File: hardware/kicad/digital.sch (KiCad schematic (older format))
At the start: 0 parts

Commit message: Added Modex library and hierarchial sheets for power, analog and digital circuitry.
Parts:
- added U?: DSPIC33FJ128GP204, QFN/TQFP44, symbol DSPIC33FJ128GP204
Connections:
- net labels added: p3v3
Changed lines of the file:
@@
 LIBS:valves
 LIBS:microchip_dspic33dsc
+LIBS:modex
 LIBS:ultrasonic_anemometer-cache
 EELAYER 25 0
@@
 $Descr A4 11693 8268
 encoding utf-8
-Sheet 1 4
+Sheet 4 4
 Title ""
 Date ""
@@
 Comment4 ""
 $EndDescr
+Text HLabel 4850 1950 0    60   Input ~ 0
+p3v3
+$Comp
+L DSPIC33FJ128GP204 U?
+U 1 1 57FA7486
+P 6250 4300
+F 0 "U?" H 5100 6350 50  0000 L CNN
+F 1 "DSPIC33FJ128GP204" H 5100 6250 50  0000 L CNN
+F 2 "QFN/TQFP44" H 6250 3500 50  0000 C CIN
+F 3 "" H 5550 3900 50  0000 C CNN
+	1    6250 4300
+	1    0    0    -1
+$EndComp
 $EndSCHEMATC

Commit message: Added symbol for DSPIC
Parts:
- removed U?: DSPIC33FJ128GP204, QFN/TQFP44, symbol DSPIC33FJ128GP204
- added U?: DSPIC33EP512GP504, QFN/TQFP44, symbol DSPIC33EP512GP504
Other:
- note added: "33EP512GP504-IPT"
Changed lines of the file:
@@
 Text HLabel 4850 1950 0    60   Input ~ 0
 p3v3
+Text Notes 1950 1700 0    60   ~ 0
+33EP512GP504-IPT
 $Comp
-L DSPIC33FJ128GP204 U?
-U 1 1 57FA7486
-P 6250 4300
-F 0 "U?" H 5100 6350 50  0000 L CNN
-F 1 "DSPIC33FJ128GP204" H 5100 6250 50  0000 L CNN
-F 2 "QFN/TQFP44" H 6250 3500 50  0000 C CIN
-F 3 "" H 5550 3900 50  0000 C CNN
-	1    6250 4300
+L DSPIC33EP512GP504 U?
+U 1 1 584BE23E
+P 6350 4100
+F 0 "U?" H 5200 6150 50  0000 L CNN
+F 1 "DSPIC33EP512GP504" H 5200 6050 50  0000 L CNN
+F 2 "QFN/TQFP44" H 6350 3300 50  0000 C CIN
+F 3 "" H 5650 3700 50  0000 C CNN
+	1    6350 4100
 	1    0    0    -1
 $EndComp

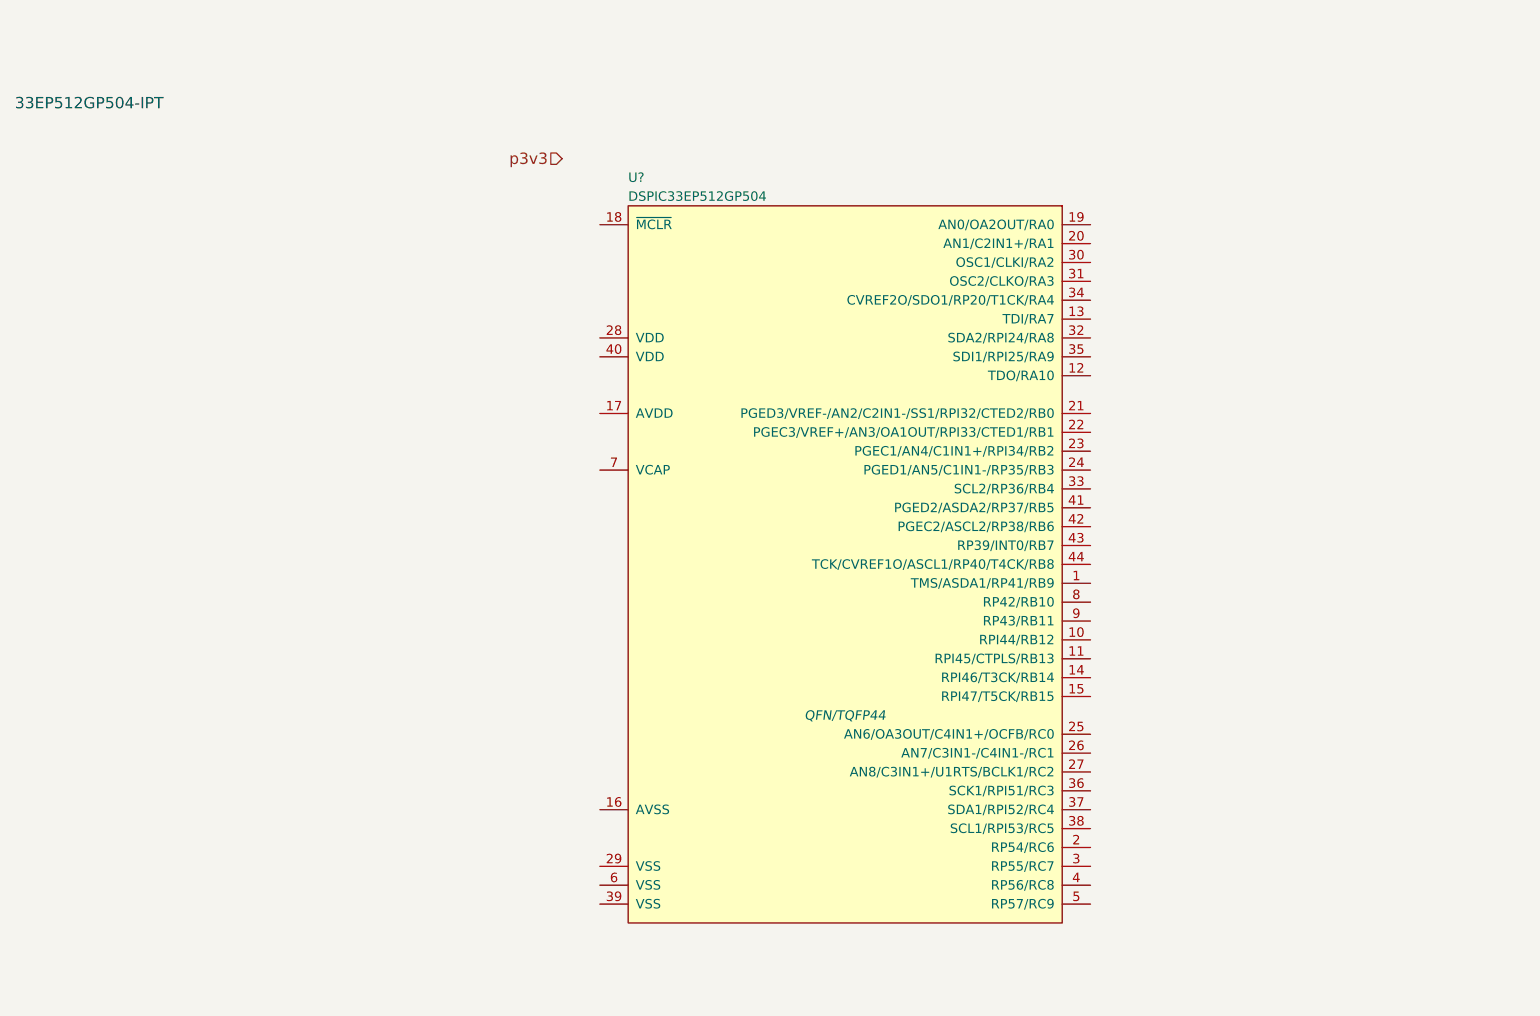
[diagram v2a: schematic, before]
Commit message: Updated schematic and PCB.
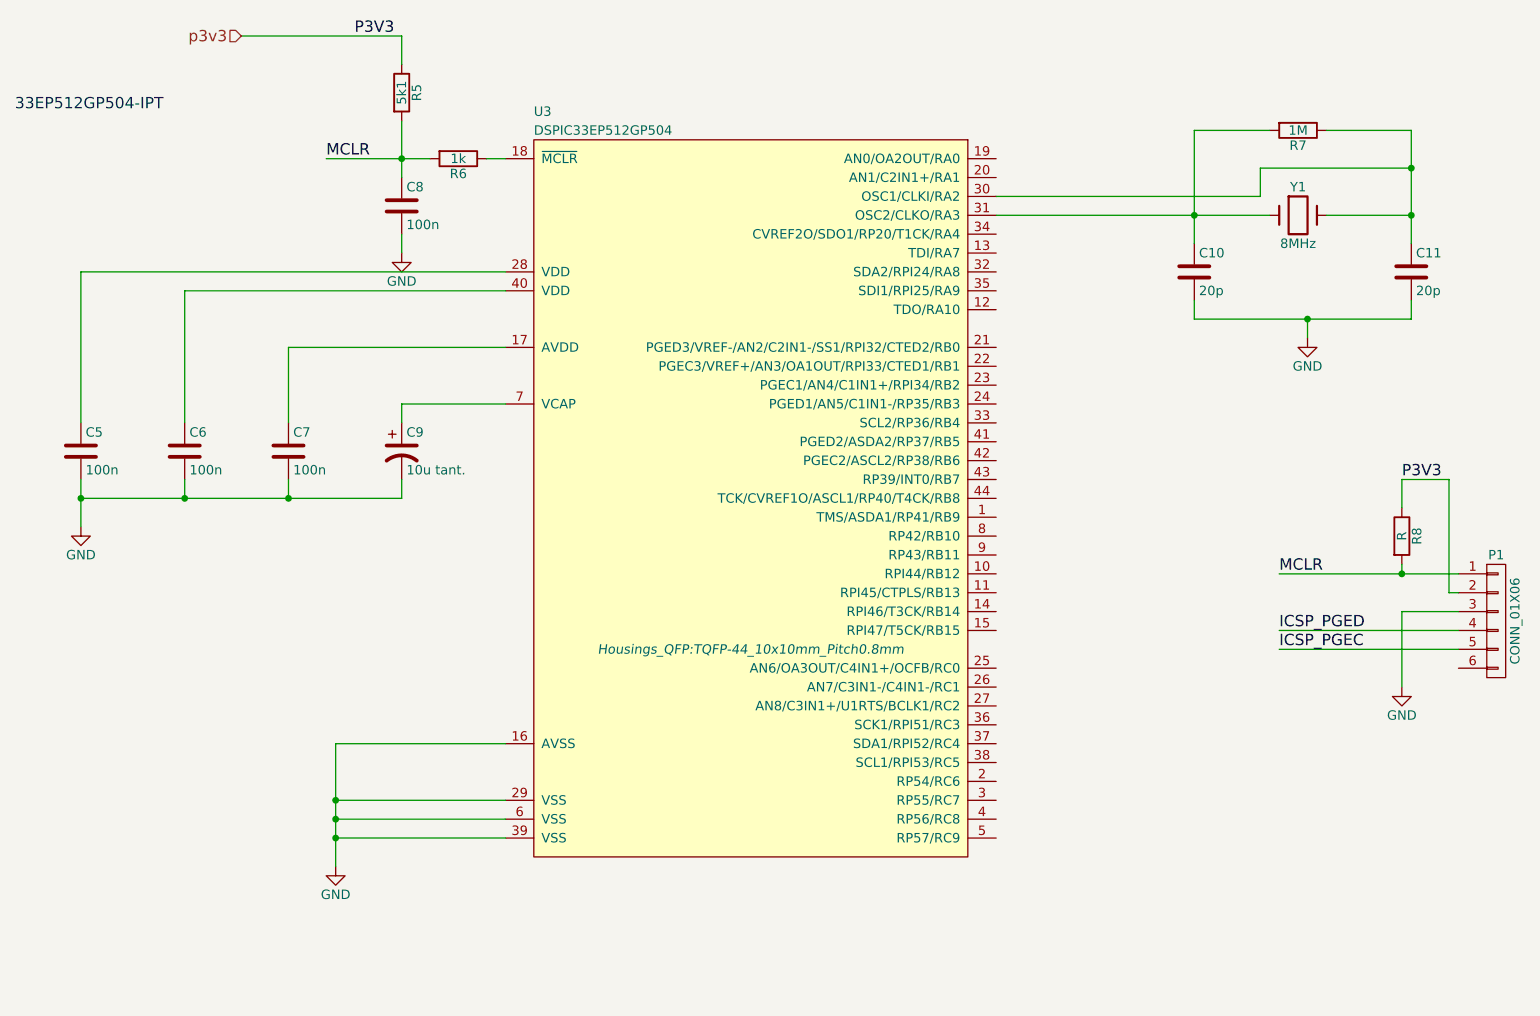
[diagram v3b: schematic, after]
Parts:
- removed U?: DSPIC33EP512GP504, QFN/TQFP44, symbol DSPIC33EP512GP504
- added C10, C11: 20p, Capacitors_SMD:C_0805_HandSoldering, symbol C
- added C5, C6, C7, C8: 100n, Capacitors_SMD:C_0805_HandSoldering, symbol C
- added C9: 10u tant., SMD_Packages:SMD-1206_Pol, symbol CP1
- added P1: CONN_01X06, Pin_Headers:Pin_Header_Straight_1x06, symbol CONN_01X06
- added R5: 5k1, Resistors_SMD:R_0805_HandSoldering, symbol R
- added R6: 1k, Resistors_SMD:R_0805_HandSoldering, symbol R
- added R7: 1M, Resistors_SMD:R_0805_HandSoldering, symbol R
- added R8: R, Resistors_SMD:R_0805_HandSoldering, symbol R
- added U3: DSPIC33EP512GP504, Housings_QFP:TQFP-44_10x10mm_Pitch0.8mm, symbol DSPIC33EP512GP504
- added Y1: 8MHz, Crystals:Crystal_HC35-U, symbol Crystal
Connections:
- net p3v3: now also P1.2 (P2), R5.1, R8.1
- new net: C7.1, U3.17 (AVDD)
- new net: R6.1, U3.18 (~MCLR)
- new net: C5.1, U3.28 (VDD)
- new net: C11.1, R7.1, U3.30 (OSC1/CLKI/RA2), Y1.2
- new net: C10.1, R7.2, U3.31 (OSC2/CLKO/RA3), Y1.1
- new net: C6.1, U3.40 (VDD)
- new net: C9.1, U3.7 (VCAP)
- new net GND: C10.2, C11.2, C5.2, C6.2, C7.2, C8.2, C9.2, P1.3 (P3), U3.16 (AVSS), U3.29 (VSS), U3.39 (VSS), U3.6 (VSS)
- new net ICSP_PGEC: P1.5 (P5)
- new net ICSP_PGED: P1.4 (P4)
- new net MCLR: C8.1, P1.1 (P1), R5.2, R6.2, R8.2

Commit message: Updated schematic and PCB. Added OPAMP to the Modex library.
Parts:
- Y1: footprint Crystals:Crystal_HC35-U -> Crystals:Crystal_HC49-SD_SMD
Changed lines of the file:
@@
 Connection ~ 2850 3750
 $Comp
-L GND #PWR011
+L GND #PWR13
 U 1 1 584BF2FB
 P 2300 3900
-F 0 "#PWR011" H 2300 3650 50  0001 C CNN
+F 0 "#PWR13" H 2300 3650 50  0001 C CNN
 F 1 "GND" H 2300 3750 50  0000 C CNN
 F 2 "" H 2300 3900 50  0000 C CNN
@@
 	4000 1750 4000 2050
 $Comp
-L GND #PWR012
+L GND #PWR15
 U 1 1 584BF583
 P 4000 2450
-F 0 "#PWR012" H 4000 2200 50  0001 C CNN
+F 0 "#PWR15" H 4000 2200 50  0001 C CNN
 F 1 "GND" H 4000 2300 50  0000 C CNN
 F 2 "" H 4000 2450 50  0000 C CNN
@@
 F 0 "Y1" H 8750 2400 50  0000 C CNN
 F 1 "8MHz" H 8750 2100 50  0000 C CNN
-F 2 "Crystals:Crystal_HC35-U" H 8750 2250 50  0001 C CNN
+F 2 "Crystals:Crystal_HC49-SD_SMD" H 8750 2250 50  0001 C CNN
 F 3 "" H 8750 2250 50  0000 C CNN
 	1    8750 2250
@@
 	9350 2800 9350 2700
 $Comp
-L GND #PWR013
+L GND #PWR16
 U 1 1 584BFE52
 P 8800 2900
-F 0 "#PWR013" H 8800 2650 50  0001 C CNN
+F 0 "#PWR16" H 8800 2650 50  0001 C CNN
 F 1 "GND" H 8800 2750 50  0000 C CNN
 F 2 "" H 8800 2900 50  0000 C CNN
@@
 Connection ~ 8800 2800
 $Comp
-L GND #PWR014
+L GND #PWR14
 U 1 1 584BFFB9
 P 3650 5700
-F 0 "#PWR014" H 3650 5450 50  0001 C CNN
+F 0 "#PWR14" H 3650 5450 50  0001 C CNN
 F 1 "GND" H 3650 5550 50  0000 C CNN
 F 2 "" H 3650 5700 50  0000 C CNN
@@
 P3V3
 $Comp
-L GND #PWR015
+L GND #PWR17
 U 1 1 584C0A98
 P 9300 4750
-F 0 "#PWR015" H 9300 4500 50  0001 C CNN
+F 0 "#PWR17" H 9300 4500 50  0001 C CNN
 F 1 "GND" H 9300 4600 50  0000 C CNN
 F 2 "" H 9300 4750 50  0000 C CNN

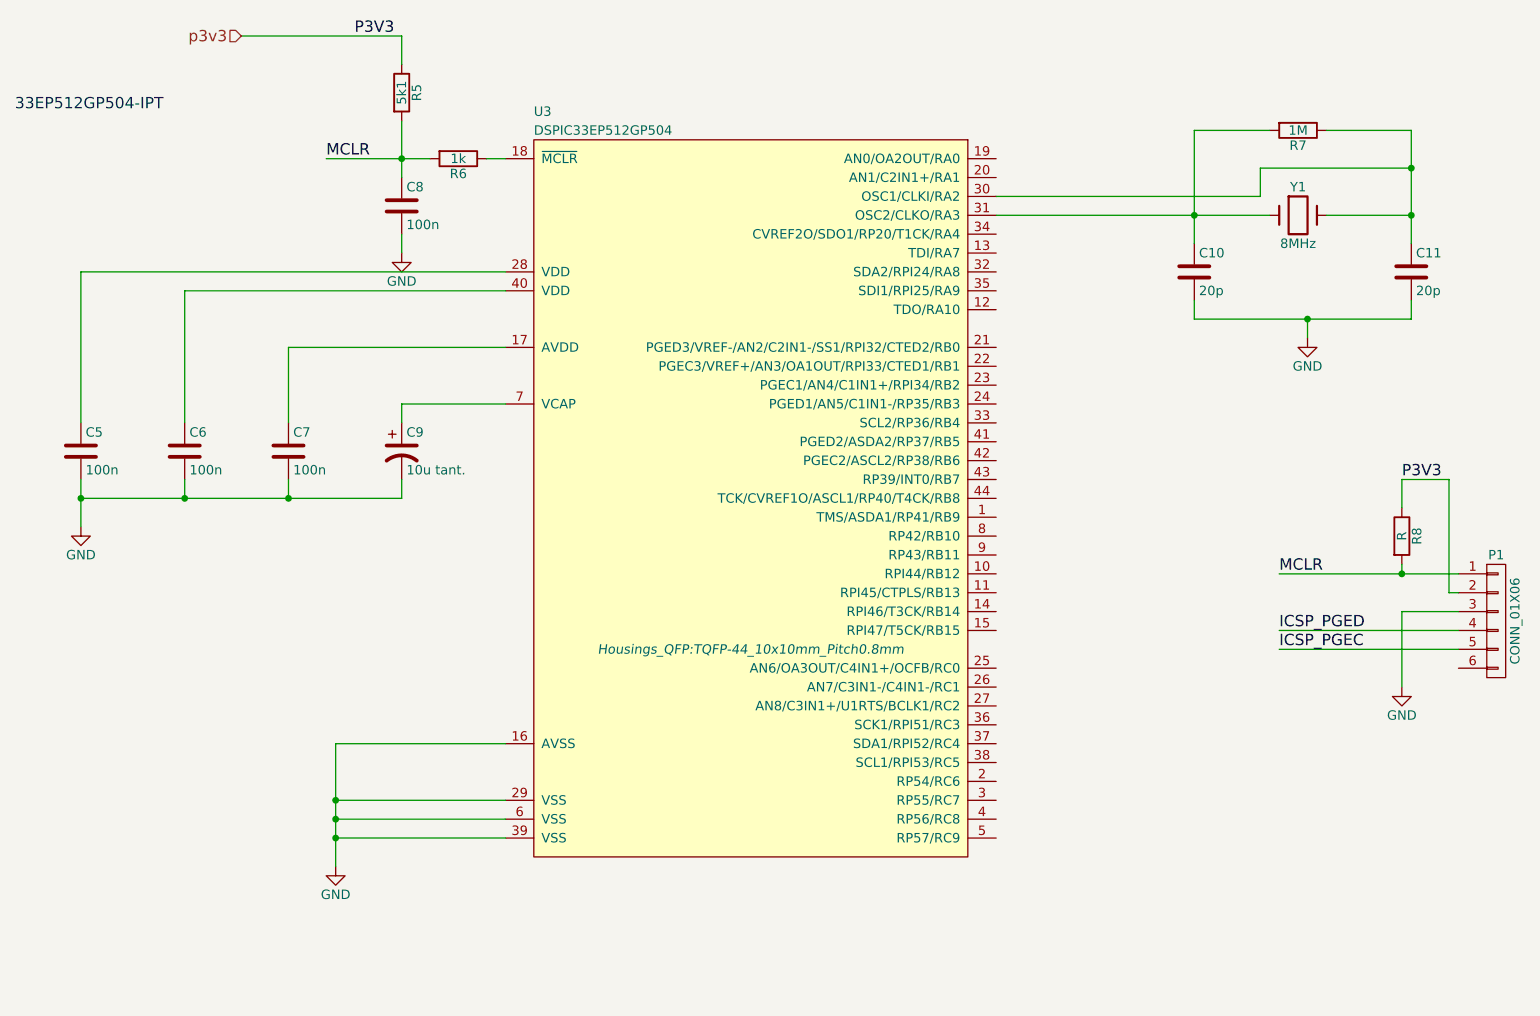
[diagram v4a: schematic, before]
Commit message: Updated schematic and PCB.
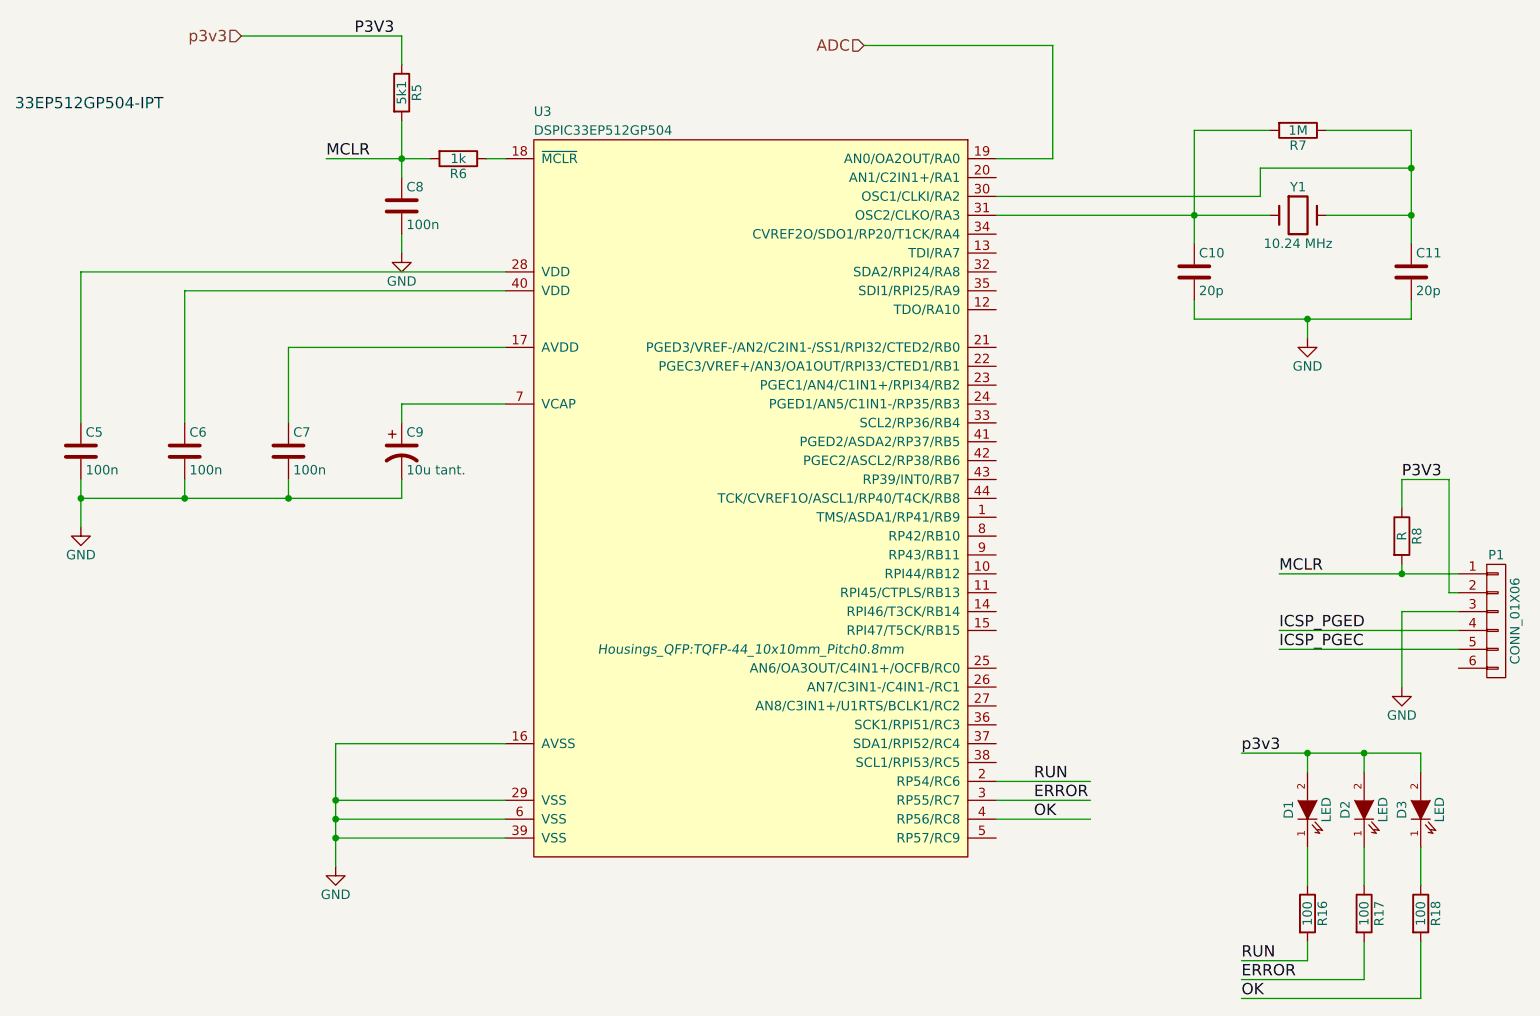
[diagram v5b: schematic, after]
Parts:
- added D1, D2, D3: LED, LEDs:LED_0805, symbol LED
- added R16, R17, R18: 100, Resistors_SMD:R_0805_HandSoldering, symbol R
- Y1: value 8MHz -> 10.24 MHz
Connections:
- net labels added: ADC, ERROR, OK, RUN
- wire segments 47 -> 66
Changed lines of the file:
@@
 Connection ~ 2850 3750
 $Comp
-L GND #PWR13
+L GND #PWR015
 U 1 1 584BF2FB
 P 2300 3900
-F 0 "#PWR13" H 2300 3650 50  0001 C CNN
+F 0 "#PWR015" H 2300 3650 50  0001 C CNN
 F 1 "GND" H 2300 3750 50  0000 C CNN
 F 2 "" H 2300 3900 50  0000 C CNN
@@
 	4000 1750 4000 2050
 $Comp
-L GND #PWR15
+L GND #PWR016
 U 1 1 584BF583
 P 4000 2450
-F 0 "#PWR15" H 4000 2200 50  0001 C CNN
+F 0 "#PWR016" H 4000 2200 50  0001 C CNN
 F 1 "GND" H 4000 2300 50  0000 C CNN
 F 2 "" H 4000 2450 50  0000 C CNN
@@
 P 8750 2250
 F 0 "Y1" H 8750 2400 50  0000 C CNN
-F 1 "8MHz" H 8750 2100 50  0000 C CNN
+F 1 "10.24 MHz" H 8750 2100 50  0000 C CNN
 F 2 "Crystals:Crystal_HC49-SD_SMD" H 8750 2250 50  0001 C CNN
 F 3 "" H 8750 2250 50  0000 C CNN
@@
 	9350 2800 9350 2700
 $Comp
-L GND #PWR16
+L GND #PWR017
 U 1 1 584BFE52
 P 8800 2900
-F 0 "#PWR16" H 8800 2650 50  0001 C CNN
+F 0 "#PWR017" H 8800 2650 50  0001 C CNN
 F 1 "GND" H 8800 2750 50  0000 C CNN
 F 2 "" H 8800 2900 50  0000 C CNN
@@
 Connection ~ 8800 2800
 $Comp
-L GND #PWR14
+L GND #PWR018
 U 1 1 584BFFB9
 P 3650 5700
-F 0 "#PWR14" H 3650 5450 50  0001 C CNN
+F 0 "#PWR018" H 3650 5450 50  0001 C CNN
 F 1 "GND" H 3650 5550 50  0000 C CNN
 F 2 "" H 3650 5700 50  0000 C CNN
@@
 P3V3
 $Comp
-L GND #PWR17
+L GND #PWR019
 U 1 1 584C0A98
 P 9300 4750
-F 0 "#PWR17" H 9300 4500 50  0001 C CNN
+F 0 "#PWR019" H 9300 4500 50  0001 C CNN
 F 1 "GND" H 9300 4600 50  0000 C CNN
 F 2 "" H 9300 4750 50  0000 C CNN
@@
 Text Label 8650 4550 0    60   ~ 0
 ICSP_PGEC
+Wire Wire Line
+	7150 1950 7450 1950
+Wire Wire Line
+	7450 1950 7450 1350
+Wire Wire Line
+	7450 1350 6450 1350
+Text HLabel 6450 1350 0    60   Input ~ 0
+ADC
+$Comp
+L LED D1
+U 1 1 5865377F
+P 8800 5400
+F 0 "D1" H 8800 5500 50  0000 C CNN
+F 1 "LED" H 8800 5300 50  0000 C CNN
+F 2 "LEDs:LED_0805" H 8800 5400 50  0001 C CNN
+F 3 "" H 8800 5400 50  0000 C CNN
+	1    8800 5400
+	0    -1   -1   0
+$EndComp
+$Comp
+L LED D2
+U 1 1 58653862
+P 9100 5400
+F 0 "D2" H 9100 5500 50  0000 C CNN
+F 1 "LED" H 9100 5300 50  0000 C CNN
+F 2 "LEDs:LED_0805" H 9100 5400 50  0001 C CNN
+F 3 "" H 9100 5400 50  0000 C CNN
+	1    9100 5400
+	0    -1   -1   0
+$EndComp
+$Comp
+L LED D3
+U 1 1 586538B1
+P 9400 5400
+F 0 "D3" H 9400 5500 50  0000 C CNN
+F 1 "LED" H 9400 5300 50  0000 C CNN
+F 2 "LEDs:LED_0805" H 9400 5400 50  0001 C CNN
+F 3 "" H 9400 5400 50  0000 C CNN
+	1    9400 5400
+	0    -1   -1   0
+$EndComp
+$Comp
+L R R16
+U 1 1 58653996
+P 8800 5950
+F 0 "R16" V 8880 5950 50  0000 C CNN
+F 1 "100" V 8800 5950 50  0000 C CNN
+F 2 "Resistors_SMD:R_0805_HandSoldering" V 8730 5950 50  0001 C CNN
+F 3 "" H 8800 5950 50  0000 C CNN
+	1    8800 5950
+	1    0    0    -1
+$EndComp
+$Comp
+L R R17
+U 1 1 586539DF
+P 9100 5950
+F 0 "R17" V 9180 5950 50  0000 C CNN
+F 1 "100" V 9100 5950 50  0000 C CNN
+F 2 "Resistors_SMD:R_0805_HandSoldering" V 9030 5950 50  0001 C CNN
+F 3 "" H 9100 5950 50  0000 C CNN
+	1    9100 5950
+	1    0    0    -1
+$EndComp
+$Comp
+L R R18
+U 1 1 58653A42
+P 9400 5950
+F 0 "R18" V 9480 5950 50  0000 C CNN
+F 1 "100" V 9400 5950 50  0000 C CNN
+F 2 "Resistors_SMD:R_0805_HandSoldering" V 9330 5950 50  0001 C CNN
+F 3 "" H 9400 5950 50  0000 C CNN
+	1    9400 5950
+	1    0    0    -1
+$EndComp
+Wire Wire Line
+	8450 5100 9400 5100
+Wire Wire Line
+	9400 5100 9400 5200
+Wire Wire Line
+	9100 5200 9100 5100
+Connection ~ 9100 5100
+Wire Wire Line
+	8800 5200 8800 5100
+Connection ~ 8800 5100
+Wire Wire Line
+	8800 5600 8800 5800
+Wire Wire Line
+	9100 5600 9100 5800
+Wire Wire Line
+	9400 5600 9400 5800
+Wire Wire Line
+	8800 6200 8800 6100
+Wire Wire Line
+	8450 6200 8800 6200
+Wire Wire Line
+	9100 6300 9100 6100
+Wire Wire Line
+	8450 6300 9100 6300
+Wire Wire Line
+	9400 6400 9400 6100
+Wire Wire Line
+	8450 6400 9400 6400
+Text Label 8450 5100 0    60   ~ 0
+p3v3
+Text Label 8450 6200 0    60   ~ 0
+RUN
+Text Label 8450 6300 0    60   ~ 0
+ERROR
+Text Label 8450 6400 0    60   ~ 0
+OK
+Wire Wire Line
+	7150 5250 7650 5250
+Wire Wire Line
+	7150 5350 7650 5350
+Wire Wire Line
+	7150 5450 7650 5450
+Text Label 7350 5350 0    60   ~ 0
+ERROR
+Text Label 7350 5250 0    60   ~ 0
+RUN
+Text Label 7350 5450 0    60   ~ 0
+OK
 $EndSCHEMATC
